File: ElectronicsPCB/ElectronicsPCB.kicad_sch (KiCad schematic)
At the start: 2 parts, among them J2 B4B-XH-A, U1 DEV-15583

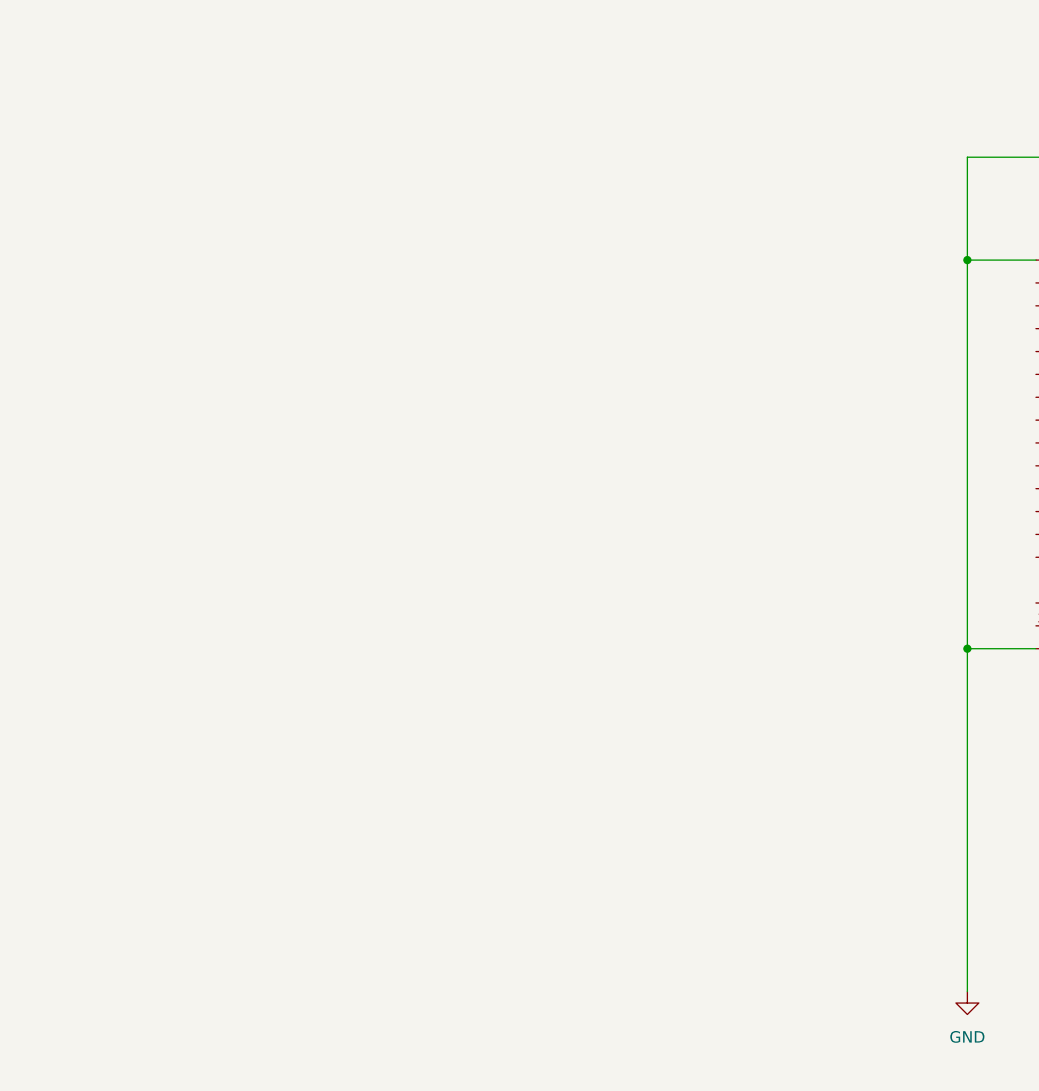
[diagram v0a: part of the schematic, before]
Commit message: made VectorNav sheet
 with '#' will be ignored, and an empty message aborts the commit.

made vectornav sheet#
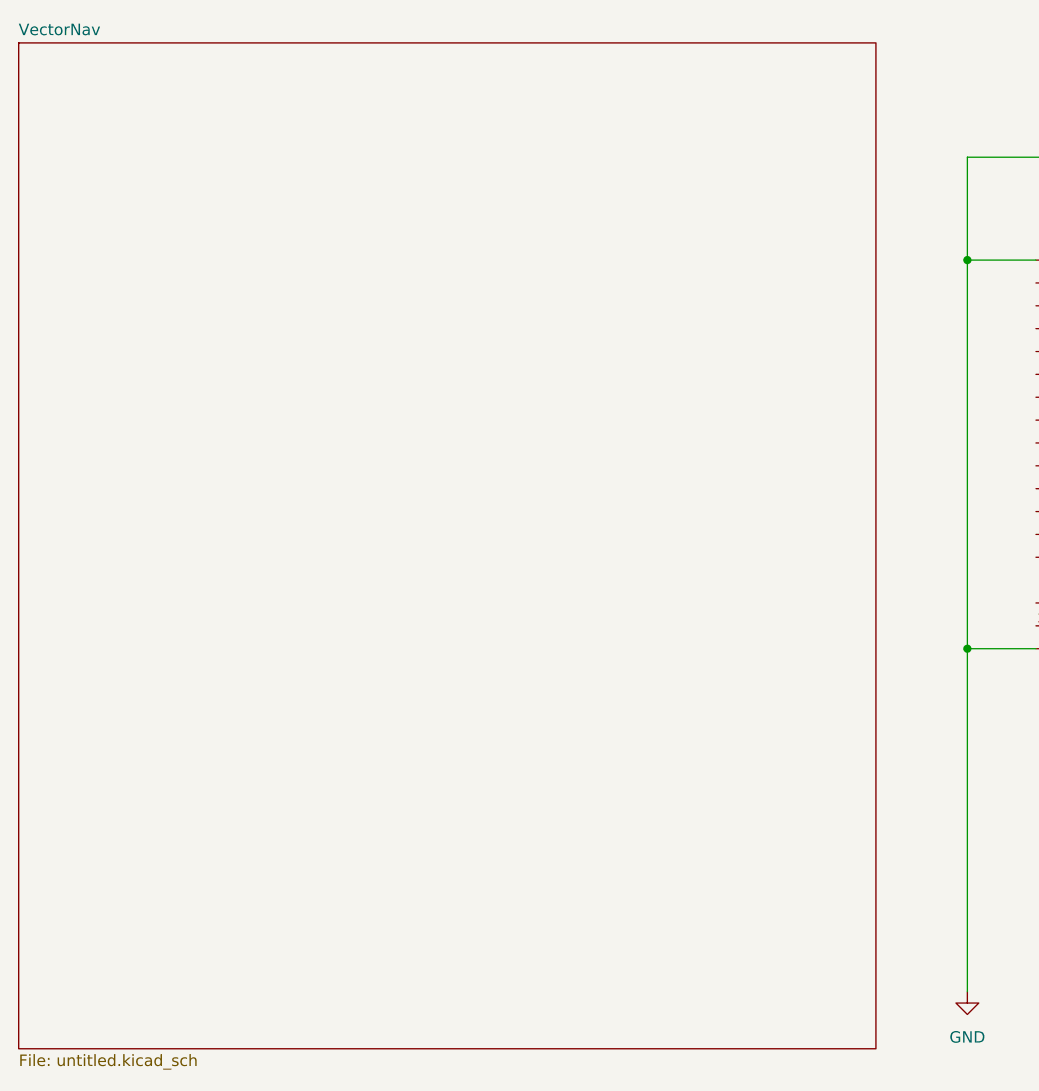
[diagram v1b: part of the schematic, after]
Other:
- added sheet VectorNav (untitled.kicad_sch)
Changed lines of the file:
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@@
+		)
+	)
+	(sheet
+		(at 20.32 20.32)
+		(size 95.25 111.76)
+		(exclude_from_sim no)
+		(in_bom yes)
+		(on_board yes)
+		(dnp no)
+		(fields_autoplaced yes)
+		(stroke
+			(width 0.1524)
+			(type solid)
+		)
+		(fill
+			(color 0 0 0 0.0000)
+		)
+		(property "Sheetname" "VectorNav"
+			(at 20.32 19.6084 0)
+			(effects
+				(font
+					(size 1.27 1.27)
+				)
+				(justify left bottom)
+			)
+		)
+		(property "Sheetfile" "untitled.kicad_sch"
+			(at 20.32 132.6646 0)
+			(effects
+				(font
+					(size 1.27 1.27)
+				)
+				(justify left top)
+			)
+		)
+		(instances
+			(project "ElectronicsPCB"
+				(path "/986f98f1-de62-46c2-9c6e-8a3d3d9a8a4d"
+					(page "2")
+				)
+			)
 		)
 	)

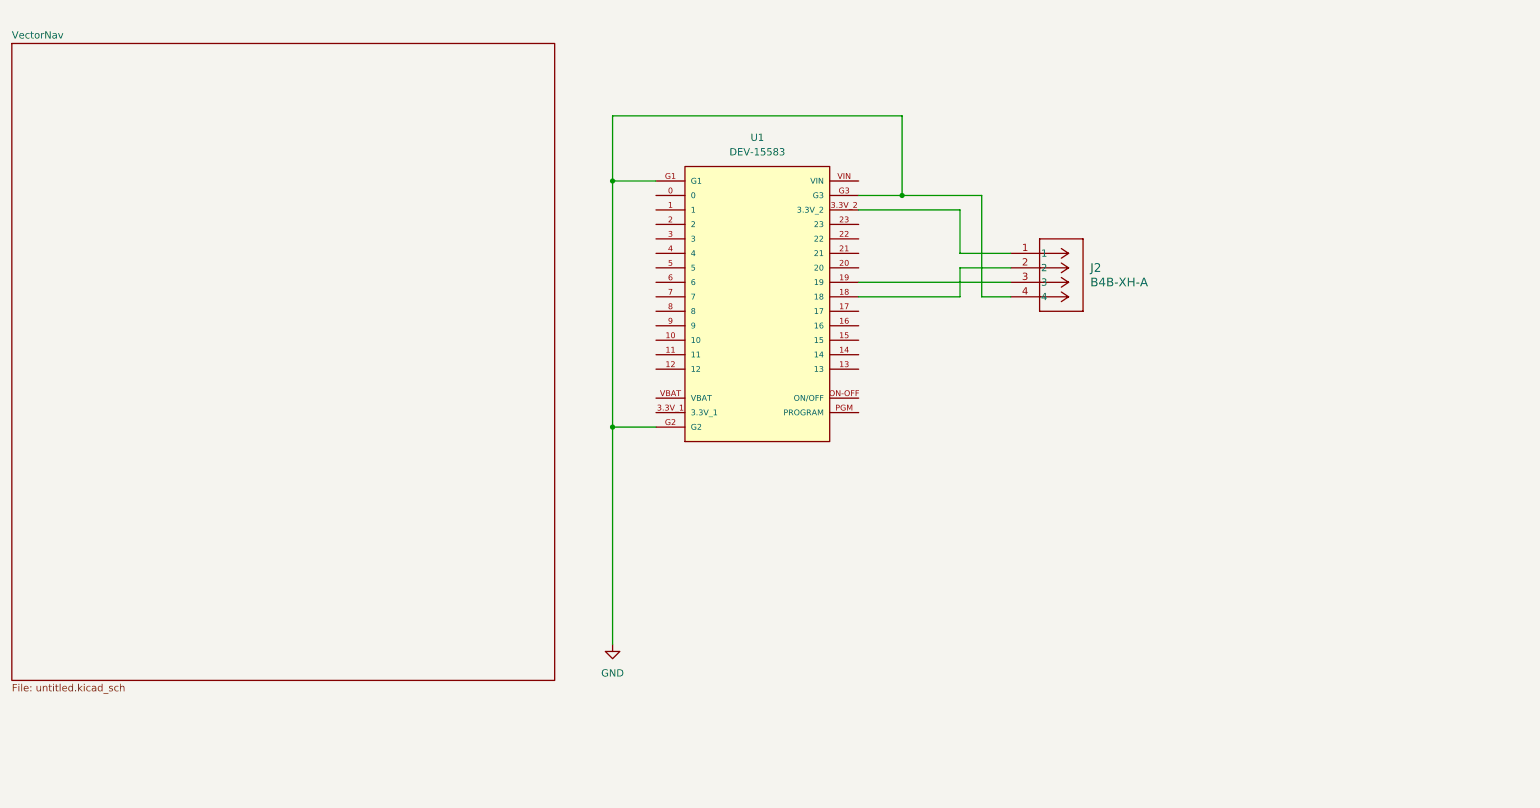
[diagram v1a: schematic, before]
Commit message: Added Teensy connections and external connectors
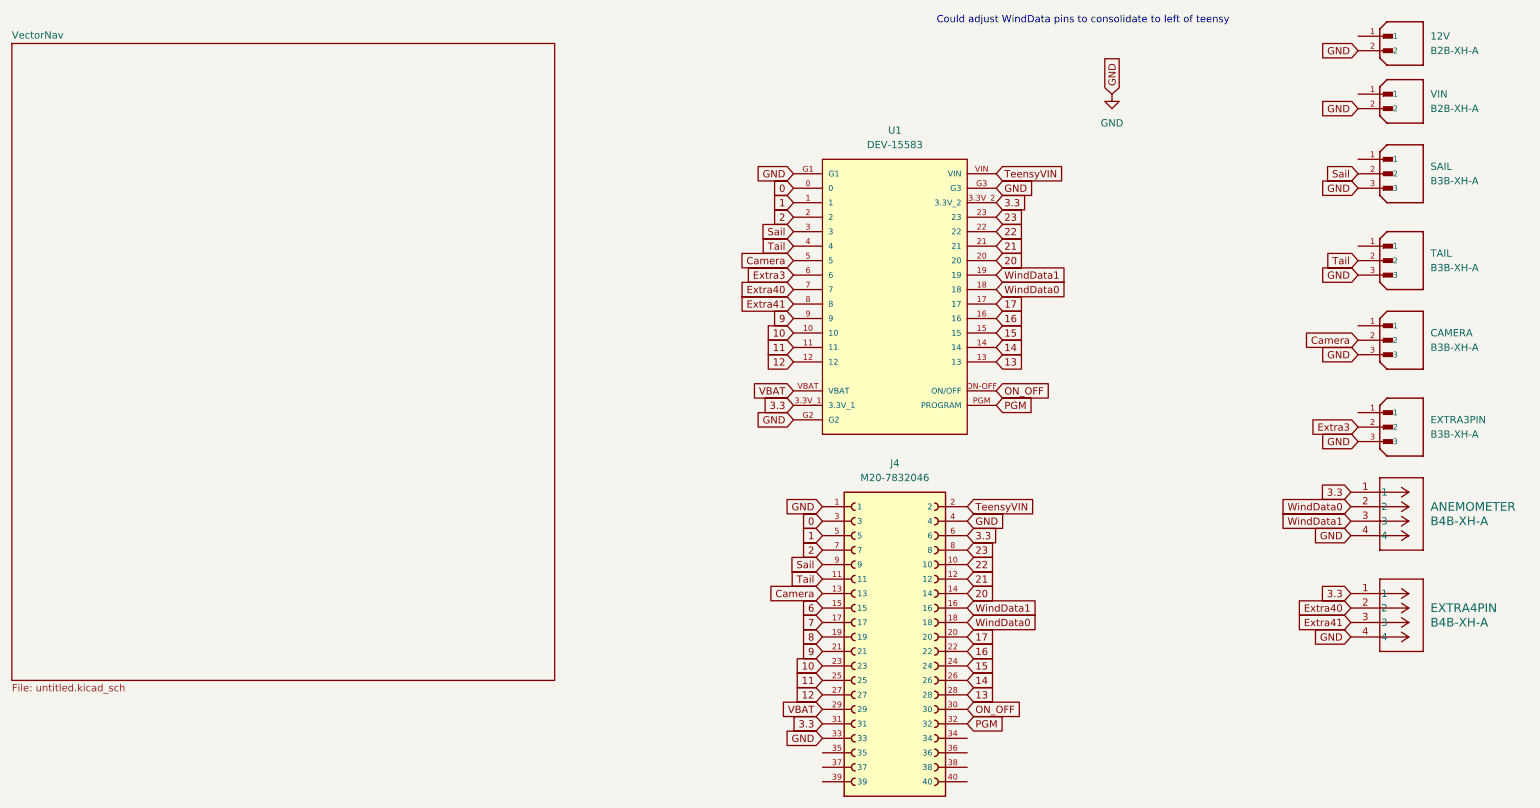
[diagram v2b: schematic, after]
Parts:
- added 12V, VIN: B2B-XH-A, B2B-XH-A:JST_B2B-XH-A, symbol 2-PinConnector:B2B-XH-A
- added CAMERA, EXTRA3PIN, SAIL, TAIL: B3B-XH-A, B3B-XH-A:JST_B3B-XH-A, symbol 3-PinConnector:B3B-XH-A
- added EXTRA4PIN: B4B-XH-A, CONN_B4B-XH-A_JST, symbol 2025-09-13_16-31-34:B4B-XH-A
- added J4: M20-7832046, M20-7832046:HARWIN_M20-7832046, symbol TeensyConnector:M20-7832046
- renumbered J2 to ANEMOMETER
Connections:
- net GND: now also 12V.2, CAMERA.3, EXTRA3PIN.3, EXTRA4PIN.4, J4.1, J4.33, J4.4, SAIL.3, TAIL.3, VIN.2
- net 0: now reaches U1.0
- net 0: now also J4.3
- net 1: now reaches U1.1
- net 1: now also J4.5
- net 10: now reaches U1.10
- net 10: now also J4.23
- net 11: now reaches U1.11
- net 11: now also J4.25
- net 12: now reaches U1.12
- net 12: now also J4.27
- net 13: now reaches U1.13
- net 13: now also J4.28
- net 14: now reaches U1.14
- net 14: now also J4.26
- net 15: now reaches U1.15
- net 15: now also J4.24
- net 16: now reaches U1.16
- net 16: now also J4.22
- net 17: now reaches U1.17
- net 17: now also J4.20
- net WindData0: now reaches ANEMOMETER.2, U1.18
- net WindData0: now also J4.18
- net WindData1: now reaches ANEMOMETER.3, U1.19
- net WindData1: now also J4.16
- net 2: now reaches U1.2
- net 2: now also J4.7
- net 20: now reaches U1.20
- net 20: now also J4.14
- net 21: now reaches U1.21
- net 21: now also J4.12
- net 22: now reaches U1.22
- net 22: now also J4.10
- net 23: now reaches U1.23
- net 23: now also J4.8
- net Sail: now reaches U1.3
- net Sail: now also J4.9, SAIL.2
- net 3.3: now reaches U1.3.3V_1
- net 3.3: now also ANEMOMETER.1, U1.3.3V_2, EXTRA4PIN.1, J4.31, J4.6
- net Tail: now reaches U1.4
- net Tail: now also J4.11, TAIL.2
- net Camera: now reaches U1.5
- net Camera: now also CAMERA.2, J4.13
- net Extra3: now reaches U1.6
- net Extra3: now also EXTRA3PIN.2
- net Extra40: now reaches U1.7
- net Extra40: now also EXTRA4PIN.2
- net Extra41: now reaches U1.8
- net Extra41: now also EXTRA4PIN.3
- net 9: now reaches U1.9
- net 9: now also J4.21
- net ON_OFF: now reaches U1.ON-OFF (ON/OFF)
- net ON_OFF: now also J4.30
- net PGM: now reaches U1.PGM (PROGRAM)
- net PGM: now also J4.32
- net VBAT: now reaches U1.VBAT
- net VBAT: now also J4.29
- net TeensyVIN: now reaches U1.VIN
- net TeensyVIN: now also J4.2
- new net 6: J4.15
- new net 7: J4.17
- new net 8: J4.19
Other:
- note added: "Could adjust WindData pins to consolidate to left of teensy"
- moved on the sheet: ANEMOMETER, U1
